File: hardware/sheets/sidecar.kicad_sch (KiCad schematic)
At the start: 6 parts, among them J1 ISA 8-bit (60p)

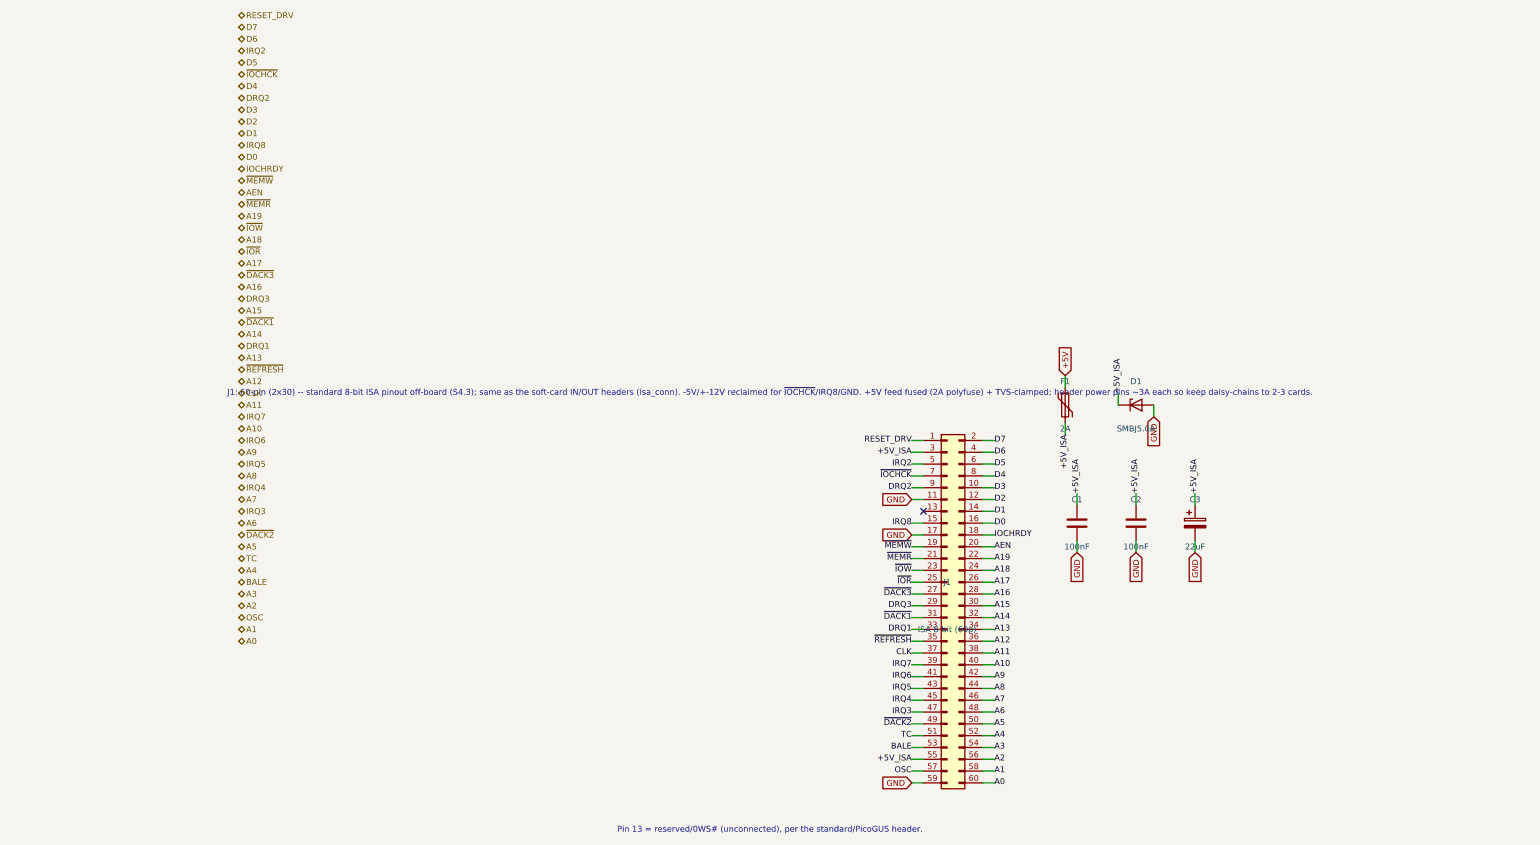
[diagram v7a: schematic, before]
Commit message: Design-review fixes: reset parking, IRQ8 off the header, analog cleanups
Netlist-wide review sweep. IRQ8 leaves the 60-pin ISA header (pin 15 is a
second GND return; the on-board RTC owns IRQ8 exclusively, so its push-pull
drive is now correct by construction). Bus MCU Hi-Z parking completed:
~CPURESET pulled low (V20 held in reset while the MCU is unprogrammed),
~DACK1/~REFRESH parked deasserted, DRQ1 idled low. Supervisor 12 MHz crystal
damping R actually in series now (was parallel-to-nothing), plus a second
USBLC6 so both prog-port SW2 positions are ESD-protected. Audio: 0.5x PG
summing (MCP6002 headroom), 100k LINE bleed, unit B parked as a follower --
and the SUM stub moved off pin 5's row, where wiring unit B would have
silently merged SUM into VREF. CH224K VDD fed through 1k per the WCH ref
design. VGA blue ladder rescaled 1k/510 -> 820/470 (was ~12% blue-deficient).
Spare CMOS gate inputs grounded uniformly (cpu_core/rtc/storage); UART_RXD
pulled up (SIN idles at mark with JP1 open); dead pins/parts dropped
(com_port CLK, parallel RESET_DRV, storage R3). Bus CLK fixed at 7.16 MHz
logged as a decision. New passives mapped to JLC basic parts in parts.py.

Co-Authored-By: Claude Fable 5 <noreply@anthropic.com>
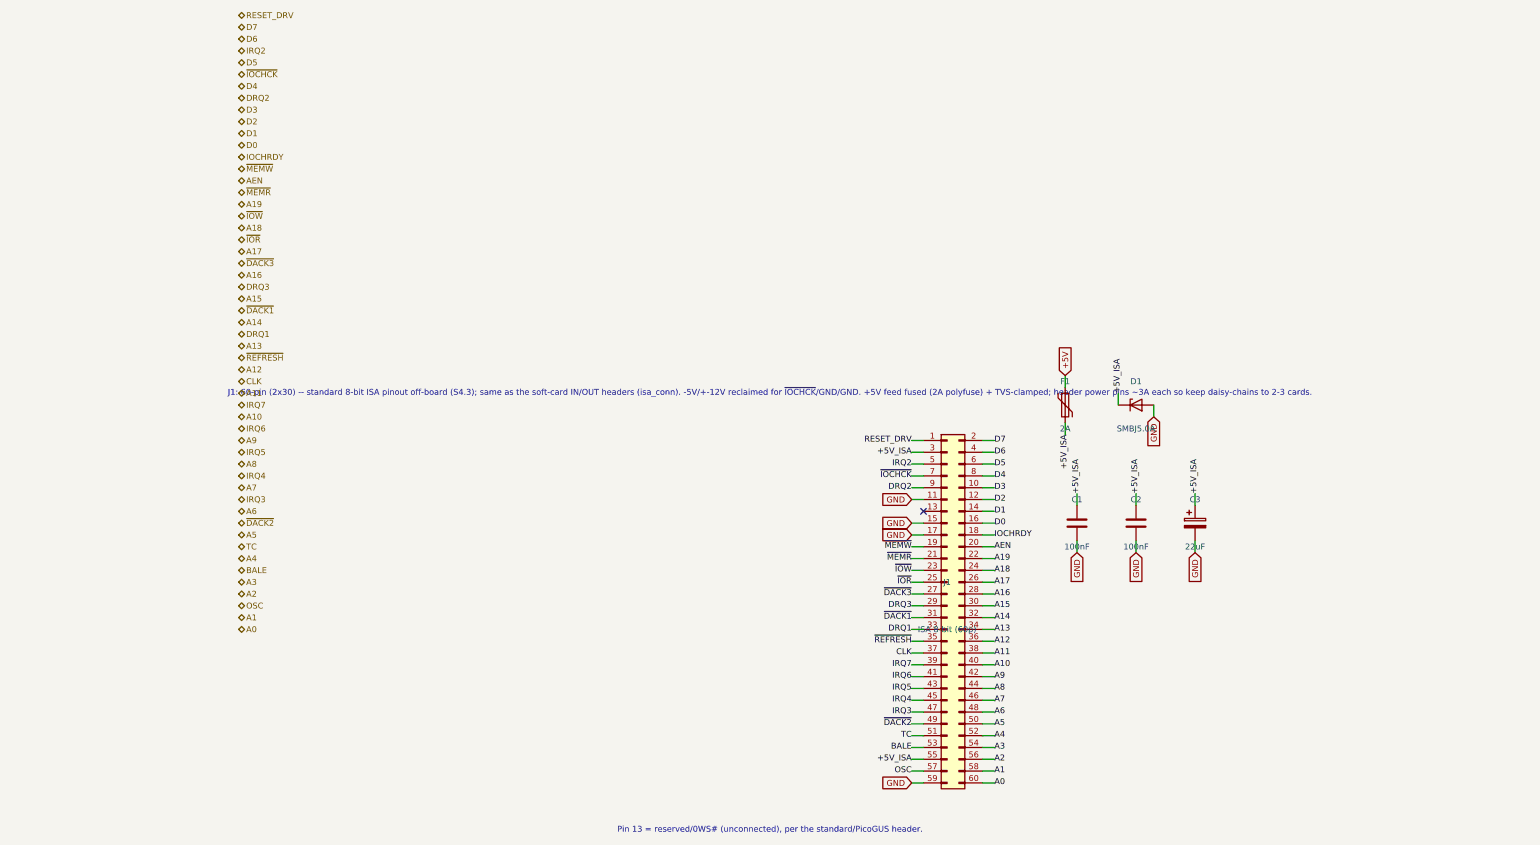
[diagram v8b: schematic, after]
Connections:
- net IRQ8 is gone; now on net GND: J1.15 (Pin_15)
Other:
- note added: "J1: 60-pin (2x30) -- standard 8-bit ISA pinout off-board (S4.3); same as the soft-card IN/OUT headers (isa_conn). -5V/+-12V reclaimed for ~{IOCHCK}/GND/GND. +5V feed fused (2A polyfuse) + TVS-clamped; header power pins ~3A each so keep daisy-chains to 2-3 cards."
- note removed: "J1: 60-pin (2x30) -- standard 8-bit ISA pinout off-board (S4.3); same as the soft-card IN/OUT headers (isa_conn). -5V/+-12V reclaimed for ~{IOCHCK}/IRQ8/GND. +5V feed fused (2A polyfuse) + TVS-clamped; header power pins ~3A each so keep daisy-chains to 2-3 cards."
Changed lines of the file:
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@@
 		)
 	)
-	(hierarchical_label "IRQ8"
+	(hierarchical_label "D0"
 		(shape bidirectional)
 		(at 25.4 53.34 0)
@@
 		)
 	)
-	(hierarchical_label "D0"
+	(hierarchical_label "IOCHRDY"
 		(shape bidirectional)
 		(at 25.4 55.88 0)
@@
 		)
 	)
-	(hierarchical_label "IOCHRDY"
+	(hierarchical_label "~{MEMW}"
 		(shape bidirectional)
 		(at 25.4 58.42 0)
@@
 		)
 	)
-	(hierarchical_label "~{MEMW}"
+	(hierarchical_label "AEN"
 		(shape bidirectional)
 		(at 25.4 60.96 0)
@@
 		)
 	)
-	(hierarchical_label "AEN"
+	(hierarchical_label "~{MEMR}"
 		(shape bidirectional)
 		(at 25.4 63.5 0)
@@
 		)
 	)
-	(hierarchical_label "~{MEMR}"
+	(hierarchical_label "A19"
 		(shape bidirectional)
 		(at 25.4 66.04 0)
@@
 		)
 	)
-	(hierarchical_label "A19"
+	(hierarchical_label "~{IOW}"
 		(shape bidirectional)
 		(at 25.4 68.58 0)
@@
 		)
 	)
-	(hierarchical_label "~{IOW}"
+	(hierarchical_label "A18"
 		(shape bidirectional)
 		(at 25.4 71.12 0)
@@
 		)
 	)
-	(hierarchical_label "A18"
+	(hierarchical_label "~{IOR}"
 		(shape bidirectional)
 		(at 25.4 73.66 0)
@@
 		)
 	)
-	(hierarchical_label "~{IOR}"
+	(hierarchical_label "A17"
 		(shape bidirectional)
 		(at 25.4 76.2 0)
@@
 		)
 	)
-	(hierarchical_label "A17"
+	(hierarchical_label "~{DACK3}"
 		(shape bidirectional)
 		(at 25.4 78.74 0)
@@
 		)
 	)
-	(hierarchical_label "~{DACK3}"
+	(hierarchical_label "A16"
 		(shape bidirectional)
 		(at 25.4 81.28 0)
@@
 		)
 	)
-	(hierarchical_label "A16"
+	(hierarchical_label "DRQ3"
 		(shape bidirectional)
 		(at 25.4 83.82 0)
@@
 		)
 	)
-	(hierarchical_label "DRQ3"
+	(hierarchical_label "A15"
 		(shape bidirectional)
 		(at 25.4 86.36 0)
@@
 		)
 	)
-	(hierarchical_label "A15"
+	(hierarchical_label "~{DACK1}"
 		(shape bidirectional)
 		(at 25.4 88.9 0)
@@
 		)
 	)
-	(hierarchical_label "~{DACK1}"
+	(hierarchical_label "A14"
 		(shape bidirectional)
 		(at 25.4 91.44 0)
@@
 		)
 	)
-	(hierarchical_label "A14"
+	(hierarchical_label "DRQ1"
 		(shape bidirectional)
 		(at 25.4 93.98 0)
@@
 		)
 	)
-	(hierarchical_label "DRQ1"
+	(hierarchical_label "A13"
 		(shape bidirectional)
 		(at 25.4 96.52 0)
@@
 		)
 	)
-	(hierarchical_label "A13"
+	(hierarchical_label "~{REFRESH}"
 		(shape bidirectional)
 		(at 25.4 99.06 0)
@@
 		)
 	)
-	(hierarchical_label "~{REFRESH}"
+	(hierarchical_label "A12"
 		(shape bidirectional)
 		(at 25.4 101.6 0)
@@
 		)
 	)
-	(hierarchical_label "A12"
+	(hierarchical_label "CLK"
 		(shape bidirectional)
 		(at 25.4 104.14 0)
@@
 		)
 	)
-	(hierarchical_label "CLK"
+	(hierarchical_label "A11"
 		(shape bidirectional)
 		(at 25.4 106.68 0)
@@
 		)
 	)
-	(hierarchical_label "A11"
+	(hierarchical_label "IRQ7"
 		(shape bidirectional)
 		(at 25.4 109.22 0)
@@
 		)
 	)
-	(hierarchical_label "IRQ7"
+	(hierarchical_label "A10"
 		(shape bidirectional)
 		(at 25.4 111.76 0)
@@
 		)
 	)
-	(hierarchical_label "A10"
+	(hierarchical_label "IRQ6"
 		(shape bidirectional)
 		(at 25.4 114.3 0)
@@
 		)
 	)
-	(hierarchical_label "IRQ6"
+	(hierarchical_label "A9"
 		(shape bidirectional)
 		(at 25.4 116.84 0)
@@
 		)
 	)
-	(hierarchical_label "A9"
+	(hierarchical_label "IRQ5"
 		(shape bidirectional)
 		(at 25.4 119.38 0)
@@
 		)
 	)
-	(hierarchical_label "IRQ5"
+	(hierarchical_label "A8"
 		(shape bidirectional)
 		(at 25.4 121.92 0)
@@
 		)
 	)
-	(hierarchical_label "A8"
+	(hierarchical_label "IRQ4"
 		(shape bidirectional)
 		(at 25.4 124.46 0)
@@
 		)
 	)
-	(hierarchical_label "IRQ4"
+	(hierarchical_label "A7"
 		(shape bidirectional)
 		(at 25.4 127 0)
@@
 		)
 	)
-	(hierarchical_label "A7"
+	(hierarchical_label "IRQ3"
 		(shape bidirectional)
 		(at 25.4 129.54 0)
@@
 		)
 	)
-	(hierarchical_label "IRQ3"
+	(hierarchical_label "A6"
 		(shape bidirectional)
 		(at 25.4 132.08 0)
@@
 		)
 	)
-	(hierarchical_label "A6"
+	(hierarchical_label "~{DACK2}"
 		(shape bidirectional)
 		(at 25.4 134.62 0)
@@
 		)
 	)
-	(hierarchical_label "~{DACK2}"
+	(hierarchical_label "A5"
 		(shape bidirectional)
 		(at 25.4 137.16 0)
@@
 		)
 	)
-	(hierarchical_label "A5"
+	(hierarchical_label "TC"
 		(shape bidirectional)
 		(at 25.4 139.7 0)
@@
 		)
 	)
-	(hierarchical_label "TC"
+	(hierarchical_label "A4"
 		(shape bidirectional)
 		(at 25.4 142.24 0)
@@
 		)
 	)
-	(hierarchical_label "A4"
+	(hierarchical_label "BALE"
 		(shape bidirectional)
 		(at 25.4 144.78 0)
@@
 		)
 	)
-	(hierarchical_label "BALE"
+	(hierarchical_label "A3"
 		(shape bidirectional)
 		(at 25.4 147.32 0)
@@
 		)
 	)
-	(hierarchical_label "A3"
+	(hierarchical_label "A2"
 		(shape bidirectional)
 		(at 25.4 149.86 0)
@@
 		)
 	)
-	(hierarchical_label "A2"
+	(hierarchical_label "OSC"
 		(shape bidirectional)
 		(at 25.4 152.4 0)
@@
 		)
 	)
-	(hierarchical_label "OSC"
+	(hierarchical_label "A1"
 		(shape bidirectional)
 		(at 25.4 154.94 0)
@@
 		)
 	)
-	(hierarchical_label "A1"
+	(hierarchical_label "A0"
 		(shape bidirectional)
 		(at 25.4 157.48 0)
-		(effects
-			(font
-				(size 1.27 1.27)
-			)
-		)
-	)
-	(hierarchical_label "A0"
-		(shape bidirectional)
-		(at 25.4 160.02 0)
 		(effects
 			(font
@@
 		)
 	)
-	(label "IRQ8"
+	(global_label "GND"
+		(shape input)
 		(at 170.18 134.62 180)
 		(effects
@@
 		)
 	)
-	(text "J1: 60-pin (2x30) -- standard 8-bit ISA pinout off-board (S4.3); same as the soft-card IN/OUT headers (isa_conn). -5V/+-12V reclaimed for ~{IOCHCK}/IRQ8/GND. +5V feed fused (2A polyfuse) + TVS-clamped; header power pins ~3A each so keep daisy-chains to 2-3 cards."
+	(text "J1: 60-pin (2x30) -- standard 8-bit ISA pinout off-board (S4.3); same as the soft-card IN/OUT headers (isa_conn). -5V/+-12V reclaimed for ~{IOCHCK}/GND/GND. +5V feed fused (2A polyfuse) + TVS-clamped; header power pins ~3A each so keep daisy-chains to 2-3 cards."
 		(at 139.7 106.68 0)
 		(effects
@@
 		(instances
 			(project "mini-xt"
-				(path "/26736c46-8b40-5460-874f-03596d17270c/16283aa1-9820-510d-8c4d-62561b97c7ba"
+				(path "/26736c46-8b40-5460-874f-03596d17270c/31a7a349-31d1-5c88-a691-60e8c25ccc60"
 					(reference "J1201")
 					(unit 1)
@@
 		(instances
 			(project "mini-xt"
-				(path "/26736c46-8b40-5460-874f-03596d17270c/16283aa1-9820-510d-8c4d-62561b97c7ba"
+				(path "/26736c46-8b40-5460-874f-03596d17270c/31a7a349-31d1-5c88-a691-60e8c25ccc60"
 					(reference "F1201")
 					(unit 1)
@@
 		(instances
 			(project "mini-xt"
-				(path "/26736c46-8b40-5460-874f-03596d17270c/16283aa1-9820-510d-8c4d-62561b97c7ba"
+				(path "/26736c46-8b40-5460-874f-03596d17270c/31a7a349-31d1-5c88-a691-60e8c25ccc60"
 					(reference "D1201")
 					(unit 1)
@@
 		(instances
 			(project "mini-xt"
-				(path "/26736c46-8b40-5460-874f-03596d17270c/16283aa1-9820-510d-8c4d-62561b97c7ba"
+				(path "/26736c46-8b40-5460-874f-03596d17270c/31a7a349-31d1-5c88-a691-60e8c25ccc60"
 					(reference "C1203")
 					(unit 1)
@@
 		(instances
 			(project "mini-xt"
-				(path "/26736c46-8b40-5460-874f-03596d17270c/16283aa1-9820-510d-8c4d-62561b97c7ba"
+				(path "/26736c46-8b40-5460-874f-03596d17270c/31a7a349-31d1-5c88-a691-60e8c25ccc60"
 					(reference "C1201")
 					(unit 1)
@@
 		(instances
 			(project "mini-xt"
-				(path "/26736c46-8b40-5460-874f-03596d17270c/16283aa1-9820-510d-8c4d-62561b97c7ba"
+				(path "/26736c46-8b40-5460-874f-03596d17270c/31a7a349-31d1-5c88-a691-60e8c25ccc60"
 					(reference "C1202")
 					(unit 1)
